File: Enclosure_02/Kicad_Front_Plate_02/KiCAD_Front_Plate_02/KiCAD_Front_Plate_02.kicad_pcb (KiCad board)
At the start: 2 copper layers, 124.8 x 50.9 mm, 0 parts

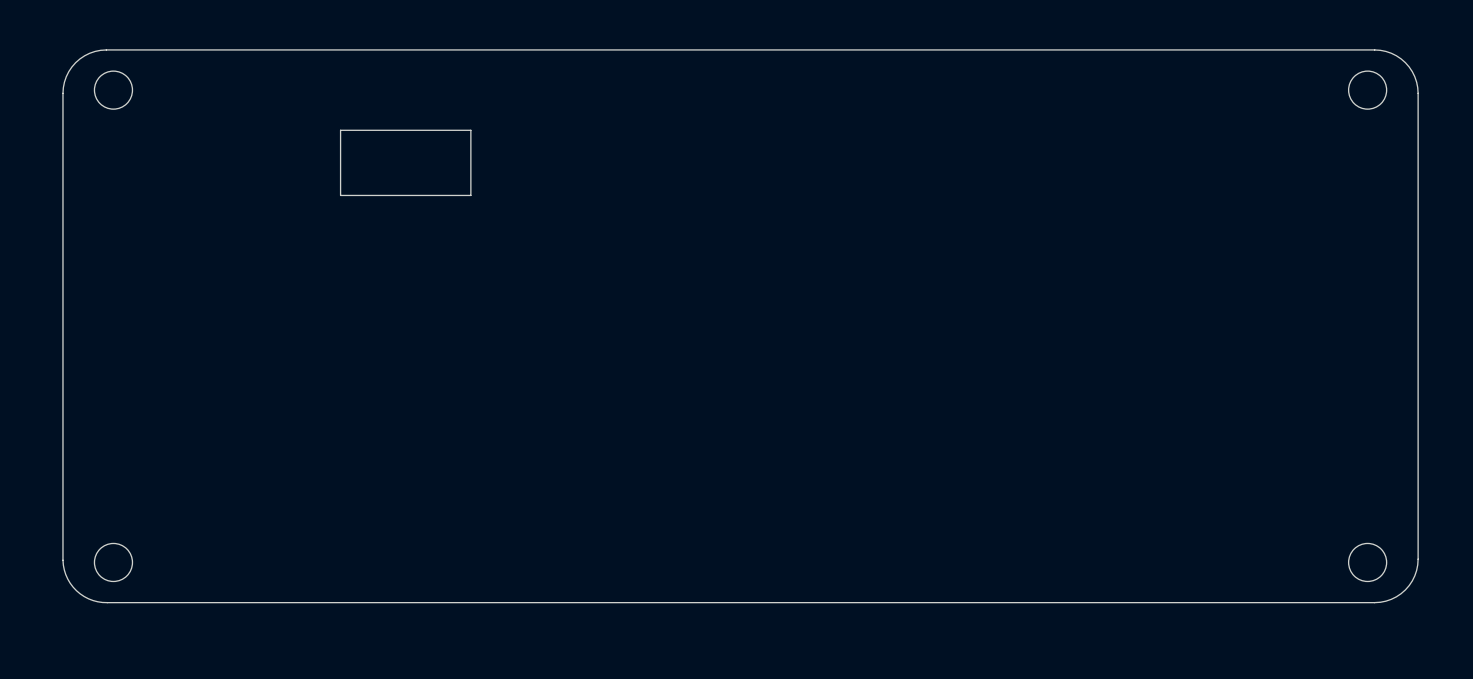
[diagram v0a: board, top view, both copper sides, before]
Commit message: Added masks to Kicad Front/back plates
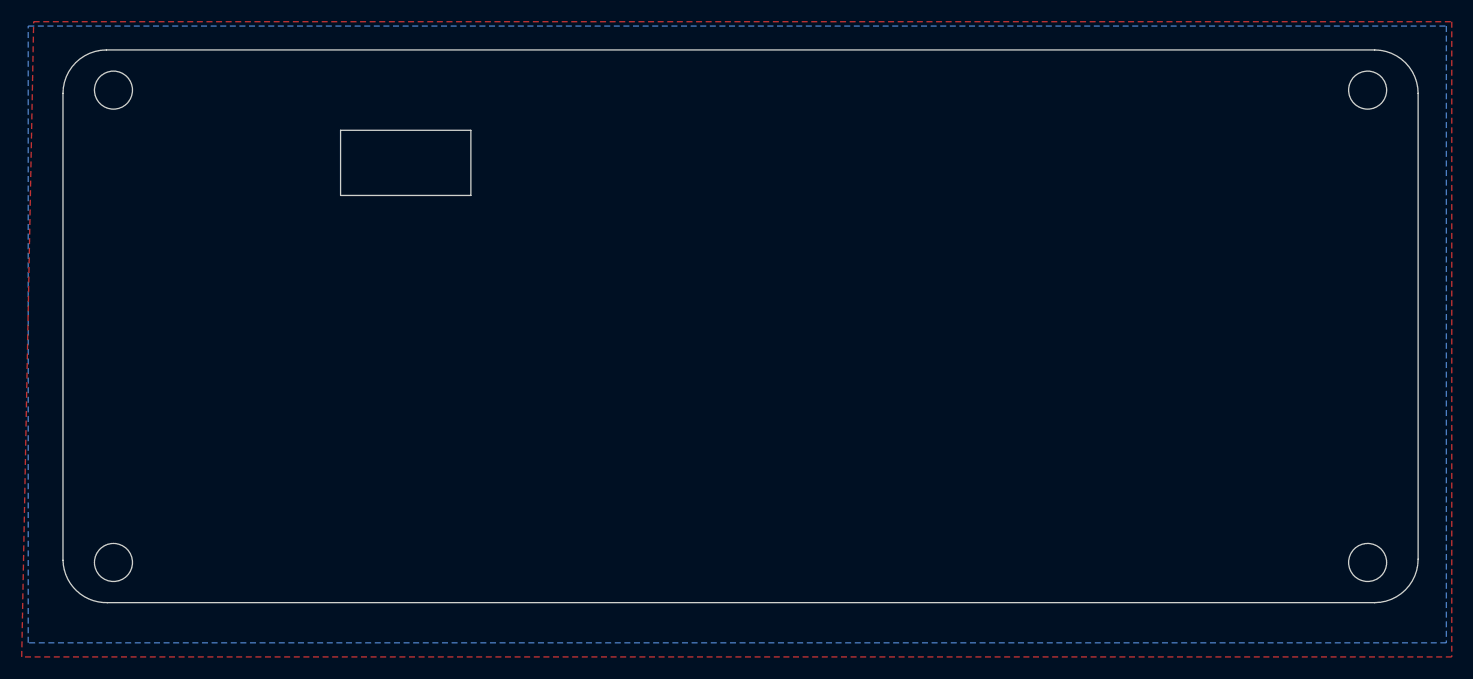
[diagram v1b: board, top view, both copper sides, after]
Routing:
- added copper zone on B.Cu, net (none)
- added copper zone on F.Cu, net (none)
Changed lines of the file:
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@@
     (pad_to_mask_clearance 0)
     (aux_axis_origin 0 0)
-    (visible_elements FFFFFF7F)
+    (visible_elements 7FFFFFFF)
     (pcbplotparams
       (layerselection 0x010fc_ffffffff)
@@
   (gr_line (start 0 4) (end 0 47) (layer Edge.Cuts) (width 0.05))
   (gr_line (start 4 0) (end 120.8 0) (layer Edge.Cuts) (width 0.05))
+  (zone (net 0) (net_name "") (layer F.Cu) (hatch edge 0.508)
+    (connect_pads (clearance 0.508))
+    (min_thickness 0.254)
+    (fill yes (arc_segments 32) (thermal_gap 0.508) (thermal_bridge_width 0.508))
+    (polygon
+      (pts
+        (xy 127.9 55.9) (xy -3.8 55.9) (xy -2.7 -2.6) (xy 127.9 -2.6)
+      )
+    )
+  )
+  (zone (net 0) (net_name "") (layer B.Cu) (hatch edge 0.508)
+    (connect_pads (clearance 0.508))
+    (min_thickness 0.254)
+    (fill yes (arc_segments 32) (thermal_gap 0.508) (thermal_bridge_width 0.508))
+    (polygon
+      (pts
+        (xy 127.4 54.6) (xy -3.2 54.6) (xy -3.2 -2.2) (xy 127.4 -2.2)
+      )
+    )
+  )
 )

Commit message: Updated mounting holes for Copper Plane and Gerber
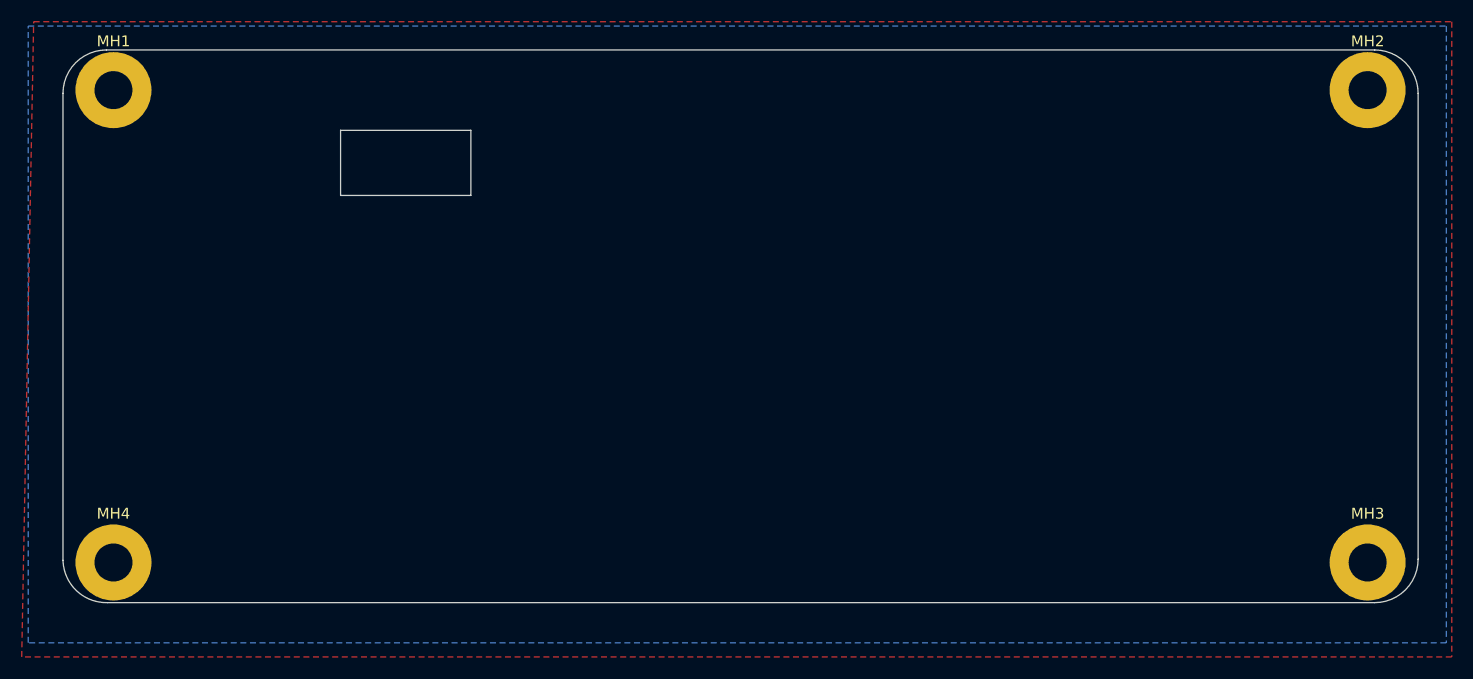
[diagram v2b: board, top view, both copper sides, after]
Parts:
- added MH1: MountingHole, MountingHole:MountingHole_3.5mm_Pad, F.Cu at (4.65, 3.70)
- added MH2: MountingHole, MountingHole:MountingHole_3.5mm_Pad, F.Cu at (120.2, 3.70)
- added MH3: MountingHole, MountingHole:MountingHole_3.5mm_Pad, F.Cu at (120.2, 47.2)
- added MH4: MountingHole, MountingHole:MountingHole_3.5mm_Pad, F.Cu at (4.65, 47.2)
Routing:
- added copper zone on B.Cu, net GND
- added copper zone on F.Cu, net GND
- removed copper zone on B.Cu, net (none)
- removed copper zone on F.Cu, net (none)
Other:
- outline, holes or cut-outs redrawn
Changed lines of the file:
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@@
   (general
     (thickness 1.6)
-    (drawings 16)
+    (drawings 12)
     (tracks 0)
     (zones 0)
-    (modules 0)
-    (nets 1)
+    (modules 4)
+    (nets 2)
   )
   (page A4)
@@
     (pcbplotparams
       (layerselection 0x010fc_ffffffff)
-      (usegerberextensions false)
-      (usegerberattributes true)
-      (usegerberadvancedattributes true)
-      (creategerberjobfile true)
+      (usegerberextensions true)
+      (usegerberattributes false)
+      (usegerberadvancedattributes false)
+      (creategerberjobfile false)
       (excludeedgelayer true)
       (linewidth 0.100000)
@@
       (psnegative false)
       (psa4output false)
-      (plotreference true)
+      (plotreference false)
       (plotvalue true)
       (plotinvisibletext false)
       (padsonsilk false)
-      (subtractmaskfromsilk false)
+      (subtractmaskfromsilk true)
       (outputformat 1)
       (mirror false)
@@
   )
   (net 0 "")
+  (net 1 GND)
   (net_class Default "This is the default net class."
     (clearance 0.2)
@@
     (uvia_dia 0.3)
     (uvia_drill 0.1)
+    (add_net GND)
   )
-  (gr_circle (center 120.15 47.2) (end 121.9 47.2) (layer Edge.Cuts) (width 0.05))
-  (gr_circle (center 4.65 47.2) (end 6.4 47.2) (layer Edge.Cuts) (width 0.05))
-  (gr_circle (center 120.15 3.7) (end 121.9 3.7) (layer Edge.Cuts) (width 0.05))
-  (gr_circle (center 4.65 3.7) (end 6.4 3.7) (layer Edge.Cuts) (width 0.05))
+  (module MountingHole:MountingHole_3.5mm_Pad (layer F.Cu)
+    (at 4.65 3.7)
+    (descr "Mounting Hole 3.5mm")
+    (tags "mounting hole 3.5mm")
+    (attr virtual)
+    (fp_text reference MH1 (at 0 -4.5) (layer F.SilkS)
+      (effects (font (size 1 1) (thickness 0.15)))
+    )
+    (fp_text value MountingHole (at 0 4.5) (layer F.Fab)
+      (effects (font (size 1 1) (thickness 0.15)))
+    )
+    (fp_circle (center 0 0) (end 3.75 0) (layer F.CrtYd) (width 0.05))
+    (fp_circle (center 0 0) (end 3.5 0) (layer Cmts.User) (width 0.15))
+    (fp_text user %R (at 0.3 0) (layer F.Fab)
+      (effects (font (size 1 1) (thickness 0.15)))
+    )
+    (pad 1 thru_hole circle (at 0 0) (size 7 7) (drill 3.5) (layers *.Cu *.Mask)
+      (net 1 GND))
+  )
+  (module MountingHole:MountingHole_3.5mm_Pad (layer F.Cu)
+    (at 120.15 3.7)
+    (descr "Mounting Hole 3.5mm")
+    (tags "mounting hole 3.5mm")
+    (attr virtual)
+    (fp_text reference MH2 (at 0 -4.5) (layer F.SilkS)
+      (effects (font (size 1 1) (thickness 0.15)))
+    )
+    (fp_text value MountingHole (at 0 4.5) (layer F.Fab)
+      (effects (font (size 1 1) (thickness 0.15)))
+    )
+    (fp_text user %R (at 0.3 0) (layer F.Fab)
+      (effects (font (size 1 1) (thickness 0.15)))
+    )
+    (fp_circle (center 0 0) (end 3.5 0) (layer Cmts.User) (width 0.15))
+    (fp_circle (center 0 0) (end 3.75 0) (layer F.CrtYd) (width 0.05))
+    (pad 1 thru_hole circle (at 0 0) (size 7 7) (drill 3.5) (layers *.Cu *.Mask)
+      (net 1 GND))
+  )
+  (module MountingHole:MountingHole_3.5mm_Pad (layer F.Cu)
+    (at 120.15 47.2)
+    (descr "Mounting Hole 3.5mm")
+    (tags "mounting hole 3.5mm")
+    (attr virtual)
+    (fp_text reference MH3 (at 0 -4.5) (layer F.SilkS)
+      (effects (font (size 1 1) (thickness 0.15)))
+    )
+    (fp_text value MountingHole (at 0 4.5) (layer F.Fab)
+      (effects (font (size 1 1) (thickness 0.15)))
+    )
+    (fp_circle (center 0 0) (end 3.75 0) (layer F.CrtYd) (width 0.05))
+    (fp_circle (center 0 0) (end 3.5 0) (layer Cmts.User) (width 0.15))
+    (fp_text user %R (at 0.3 0) (layer F.Fab)
+      (effects (font (size 1 1) (thickness 0.15)))
+    )
+    (pad 1 thru_hole circle (at 0 0) (size 7 7) (drill 3.5) (layers *.Cu *.Mask)
+      (net 1 GND))
+  )
+  (module MountingHole:MountingHole_3.5mm_Pad (layer F.Cu)
+    (at 4.65 47.2)
+    (descr "Mounting Hole 3.5mm")
+    (tags "mounting hole 3.5mm")
+    (attr virtual)
+    (fp_text reference MH4 (at 0 -4.5) (layer F.SilkS)
+      (effects (font (size 1 1) (thickness 0.15)))
+    )
+    (fp_text value MountingHole (at 0 4.5) (layer F.Fab)
+      (effects (font (size 1 1) (thickness 0.15)))
+    )
+    (fp_text user %R (at 0.3 0) (layer F.Fab)
+      (effects (font (size 1 1) (thickness 0.15)))
+    )
+    (fp_circle (center 0 0) (end 3.5 0) (layer Cmts.User) (width 0.15))
+    (fp_circle (center 0 0) (end 3.75 0) (layer F.CrtYd) (width 0.05))
+    (pad 1 thru_hole circle (at 0 0) (size 7 7) (drill 3.5) (layers *.Cu *.Mask)
+      (net 1 GND))
+  )
   (gr_arc (start 4 46.9) (end 0 47) (angle -90) (layer Edge.Cuts) (width 0.05))
   (gr_arc (start 120.8 46.9) (end 120.8 50.9) (angle -90) (layer Edge.Cuts) (width 0.05))
@@
   (gr_line (start 0 4) (end 0 47) (layer Edge.Cuts) (width 0.05))
   (gr_line (start 4 0) (end 120.8 0) (layer Edge.Cuts) (width 0.05))
-  (zone (net 0) (net_name "") (layer F.Cu) (hatch edge 0.508)
+  (zone (net 1) (net_name GND) (layer F.Cu) (hatch edge 0.508)
     (connect_pads (clearance 0.508))
     (min_thickness 0.254)
@@
     )
   )
-  (zone (net 0) (net_name "") (layer B.Cu) (hatch edge 0.508)
+  (zone (net 1) (net_name GND) (layer B.Cu) (hatch edge 0.508)
     (connect_pads (clearance 0.508))
     (min_thickness 0.254)
